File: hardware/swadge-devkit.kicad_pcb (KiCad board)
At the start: 2 copper layers, 63.7 x 89.4 mm, 65 parts, among them J1 USB_B_Micro, SW1 SW_SPDT, SW2 4-1437565-2, SW3 4-1437565-2, SW4 4-1437565-2, SW5 4-1437565-2, U1 ESP-13-WROOM-02D, U2 MCP6001-OT, U3 MSA300, U4 AP1117-33, U5 BUS_PCIexpress, U6 DISP_OLED_UG-2864HSWEG01, U7 SAO, U9 MMA8452Q

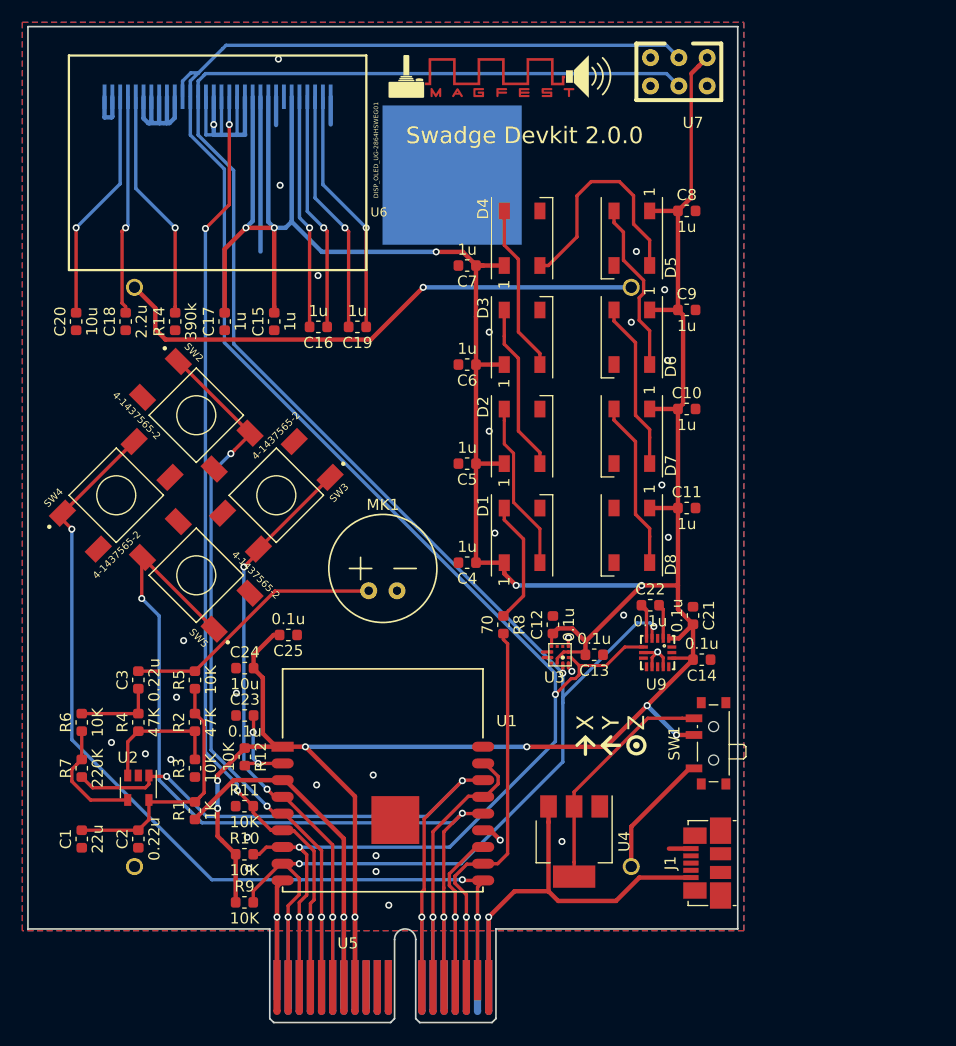
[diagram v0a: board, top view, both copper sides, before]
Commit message: Added Gainsil GS321-TR opamp
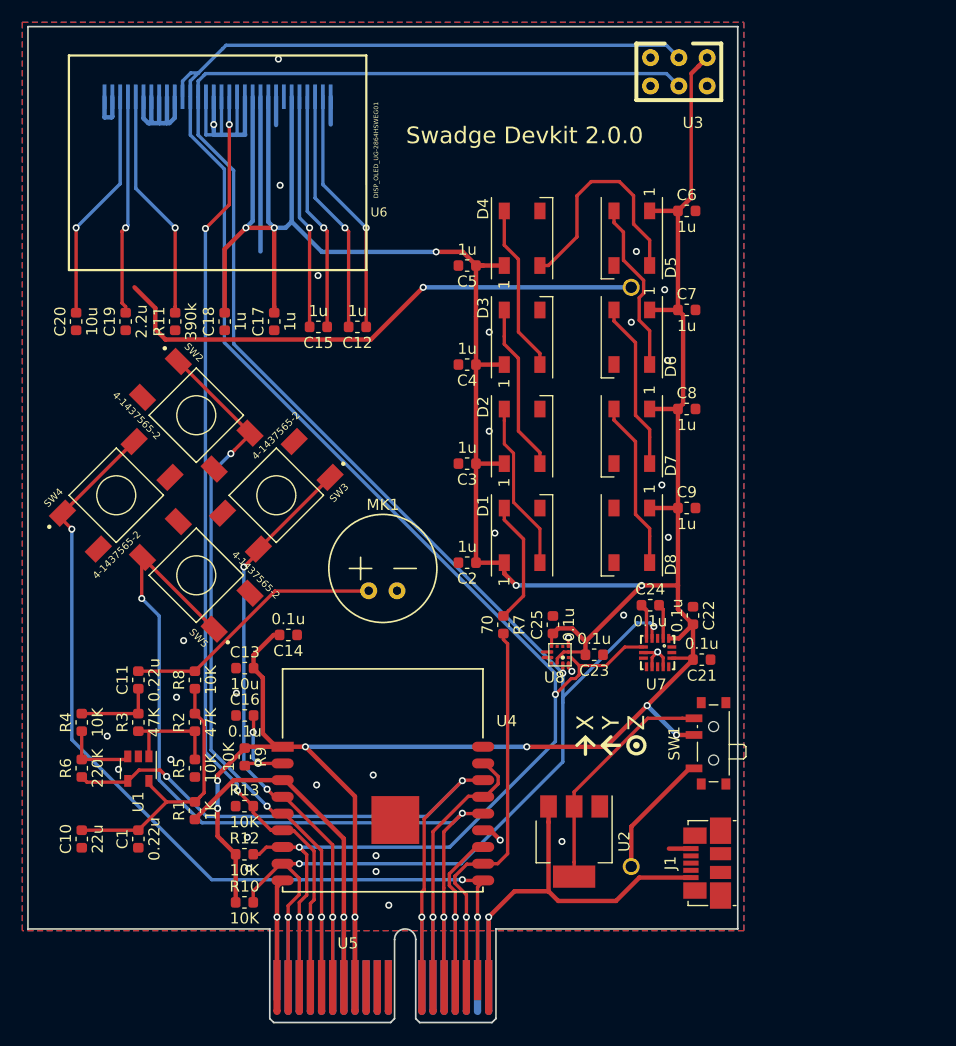
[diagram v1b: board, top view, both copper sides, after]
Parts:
- removed BT1: Battery, Swadge_Parts:2460
- removed the U2 at (123.4, 126.2)
- removed svg2mod: G***, Swadge_Parts:pcb_color_swatches
- removed svg2mod: G***, Swadge_Parts:MAGFEST_logo_centered_final
- added U1: GS321-TR, Swadge_Parts:SOT-23-5, F.Cu at (123.4, 124.5)
- renumbered C2 to C1, C1 to C10, C3 to C11, C19 to C12, C24 to C13, C25 to C14, C16 to C15, C23 to C16, C15 to C17, C17 to C18, C18 to C19, C4 to C2, C14 to C21, C21 to C22, C13 to C23, C22 to C24, C12 to C25, C5 to C3, C6 to C4, C7 to C5, C8 to C6, C9 to C7, C10 to C8, C11 to C9, R9 to R10, R14 to R11, R10 to R12, R11 to R13, R4 to R3, R6 to R4, R3 to R5, R7 to R6, R8 to R7, R5 to R8, R12 to R9, U4 to U2, U7 to U3, U1 to U4, U9 to U7, U3 to U8
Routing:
- net Net-(R4-Pad1): track 10.6 -> 6.41 mm
- net Net-(R2-Pad1): track 12.0 -> 9.89 mm
- net Net-(C1-Pad2): track 23.2 -> 24.2 mm
- net ADC_PIN: track 66.6 -> 65.7 mm

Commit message: Added back missing battery, PCB art
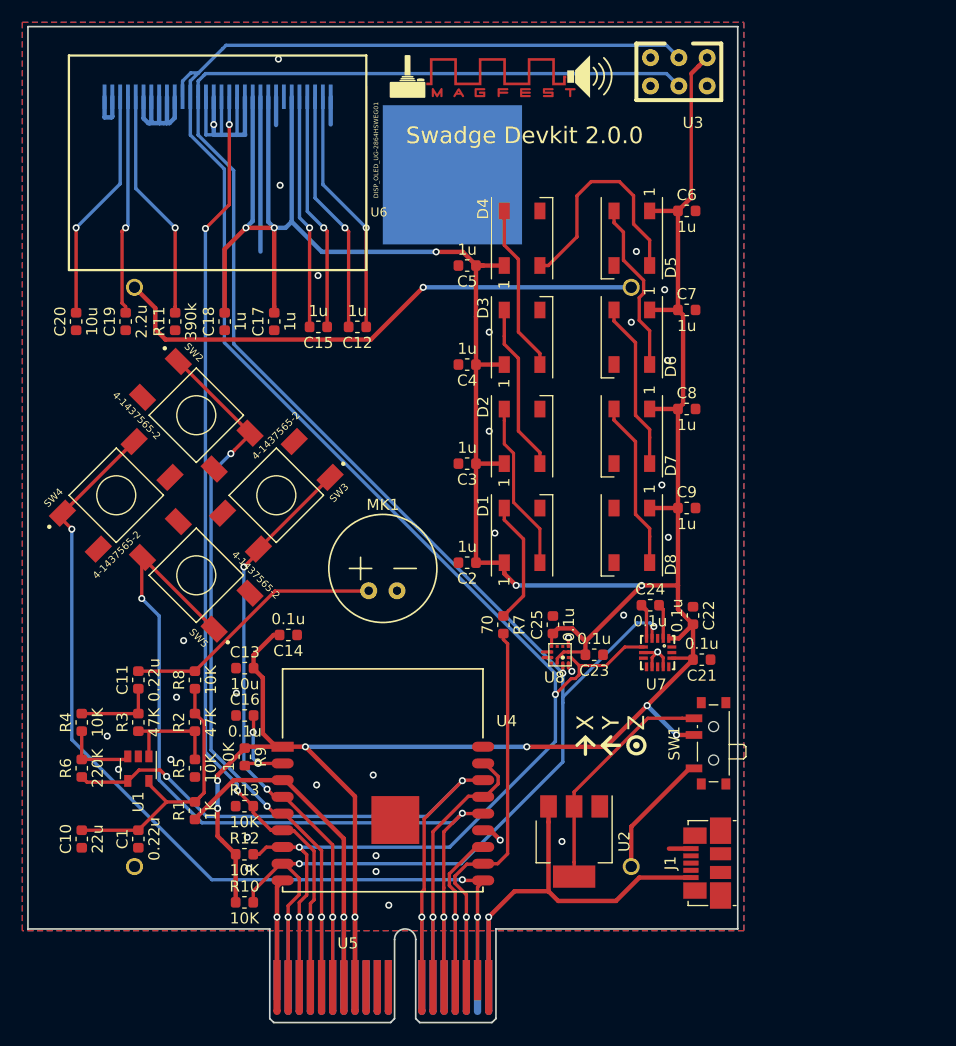
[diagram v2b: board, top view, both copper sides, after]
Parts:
- added BT1: Battery, Swadge_Parts:2460, B.Cu at (123.1, 107.3)
- added svg2mod: G***, Swadge_Parts:pcb_color_swatches, B.Cu at (157.9, 71.2)
- added svg2mod: G***, Swadge_Parts:MAGFEST_logo_centered_final, F.Cu at (156.0, 62.4)

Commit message: Added QMA6981 to the devkit
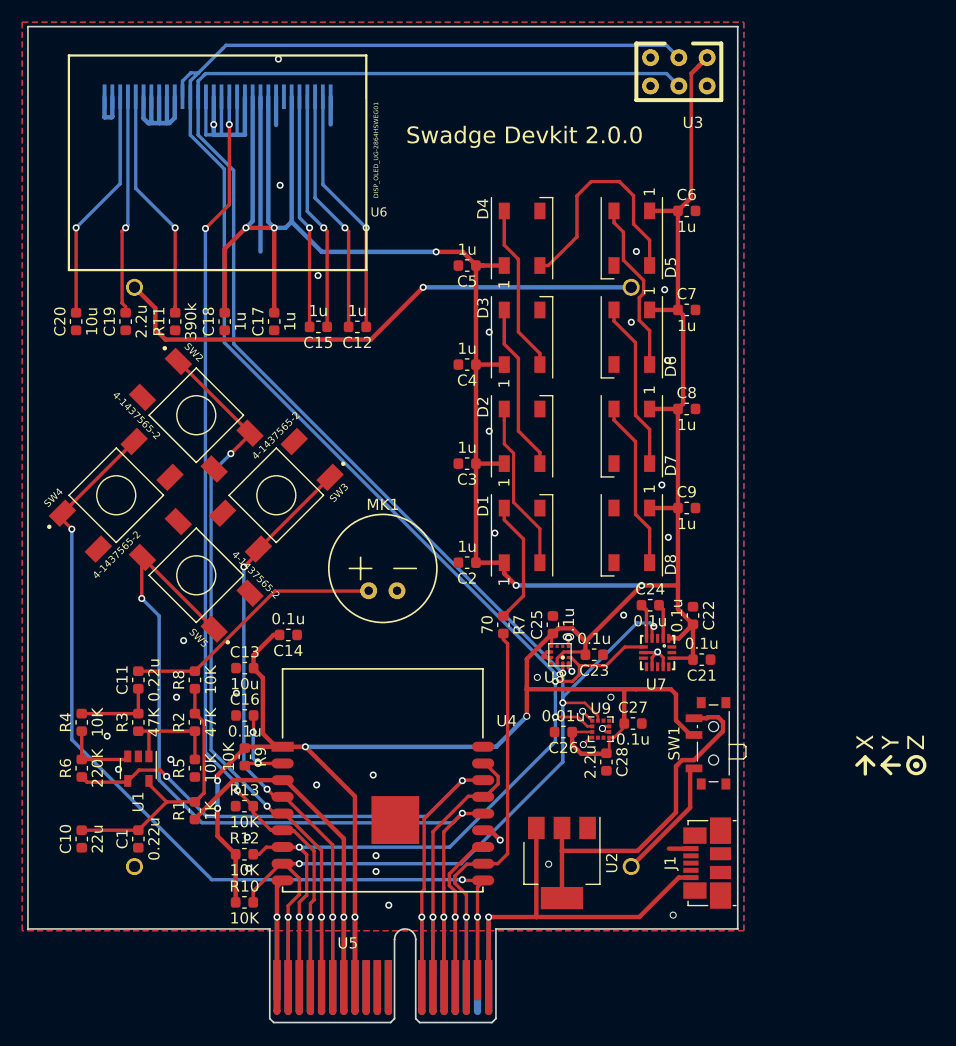
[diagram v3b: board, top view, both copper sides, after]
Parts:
- removed svg2mod: G***, Swadge_Parts:pcb_color_swatches
- removed svg2mod: G***, Swadge_Parts:MAGFEST_logo_centered_final
- added C26: 0.01u, Swadge_Parts:C_0603_1608Metric, F.Cu at (161.6, 121.2)
- added C27: 0.1u, Swadge_Parts:C_0603_1608Metric, F.Cu at (167.8, 120.5)
- added C28: 2.2u, Swadge_Parts:C_0603_1608Metric, F.Cu at (165.5, 123.9)
- added U9: QMA6981, Swadge_Parts:LGA-12_2x2mm_P0.5mm, F.Cu at (164.9, 121.0)
- moved U2 2.22 mm to (161.5, 133.0)
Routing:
- net +3V3: track 322.1 -> 338.9 mm, vias 12 -> 10
- net Net-(SW1-Pad3): track 21.1 -> 31.3 mm
- net SCL: track 184.0 -> 188.0 mm, vias 4 -> 5
- net GND: track 88.1 -> 92.0 mm, vias 33 -> 39
- net SDA: track 183.3 -> 186.3 mm, vias 3 -> 4
- net Net-(BT2-Pad1): track 11.4 -> 10.8 mm
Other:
- net class xThin added: clearance 0.19558, trace_width 0.2, via_dia 0.635, via_drill 0.3556

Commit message: Fixed silkscreen
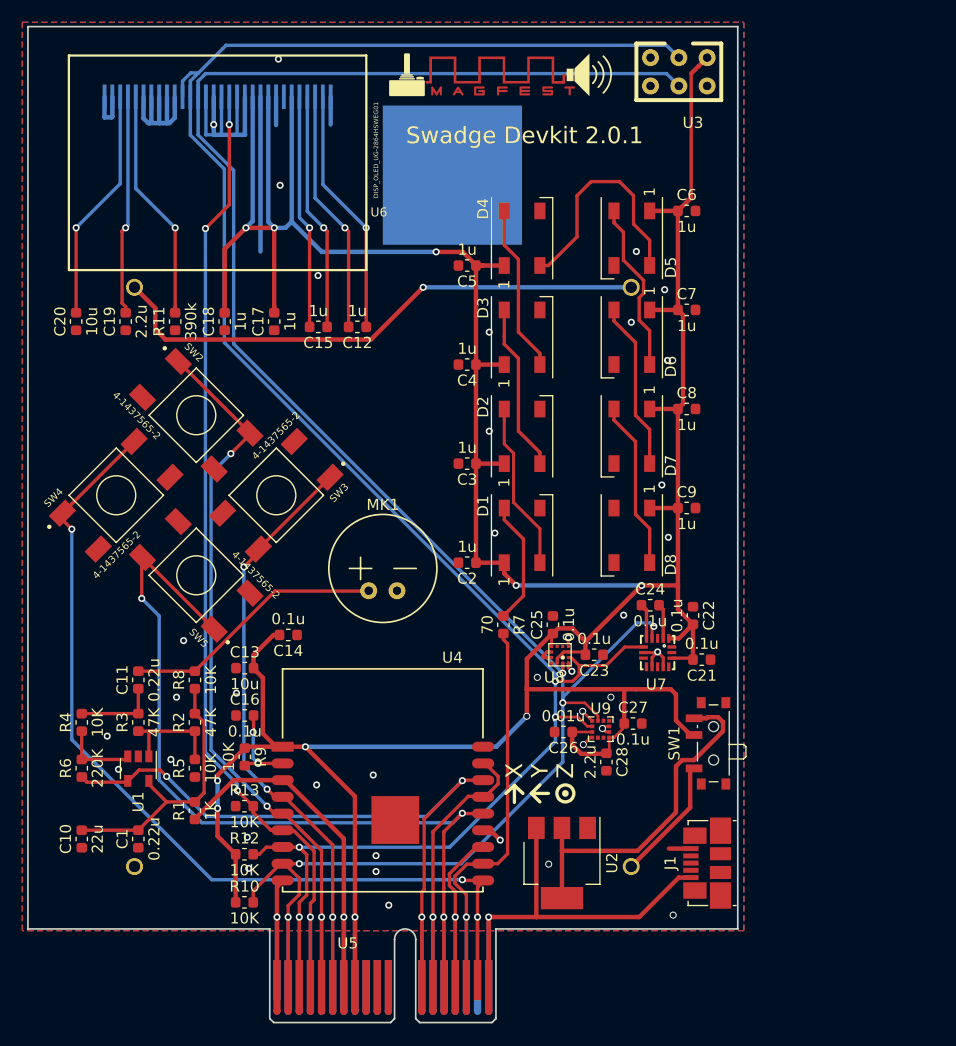
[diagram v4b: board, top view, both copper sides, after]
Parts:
- added svg2mod: G***, Swadge_Parts:pcb_color_swatches, B.Cu at (157.9, 71.2)
- added svg2mod: G***, Swadge_Parts:MAGFEST_logo_centered_final, F.Cu at (156.0, 62.2)
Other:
- board text added: "Swadge Devkit 2.0.1"
- board text removed: "Swadge Devkit 2.0.0"

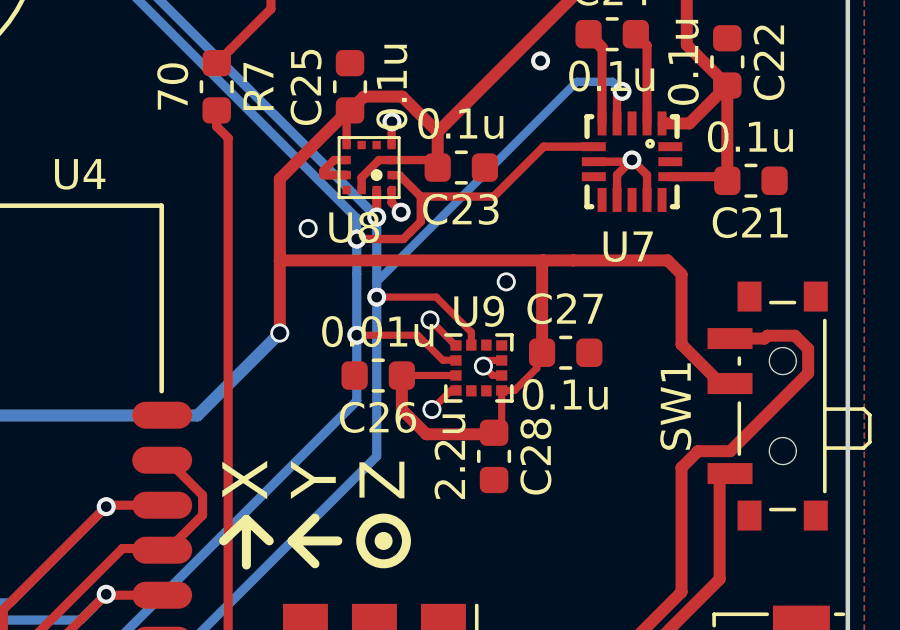
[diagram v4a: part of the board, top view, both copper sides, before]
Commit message: Added new QMA6981 footprint, no more DRC errors
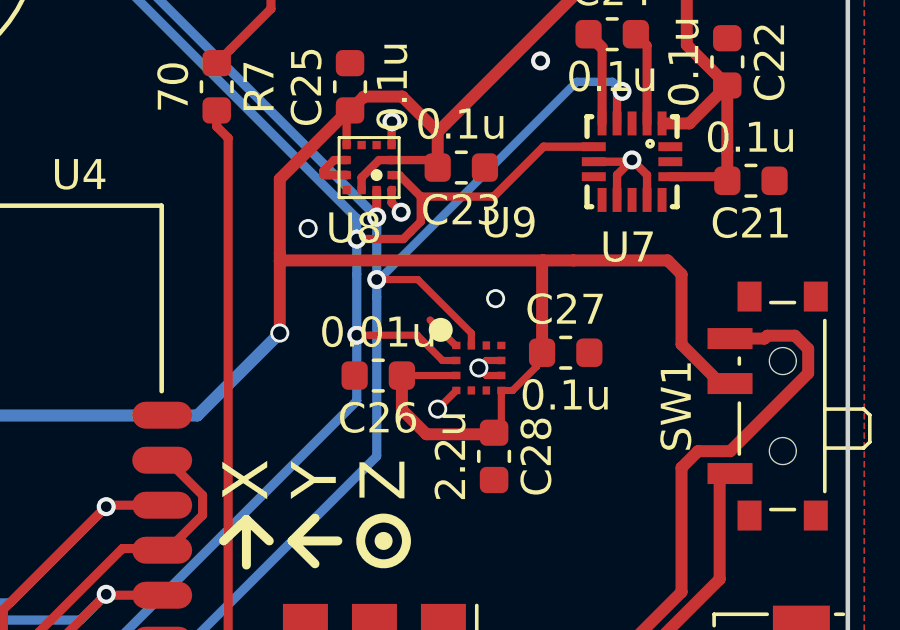
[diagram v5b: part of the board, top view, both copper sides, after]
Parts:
- U9: footprint Swadge_Parts:LGA-12_2x2mm_P0.5mm -> Swadge_Parts:QMA6981
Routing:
- net GND: track 92.0 -> 92.1 mm, vias 39 -> 38

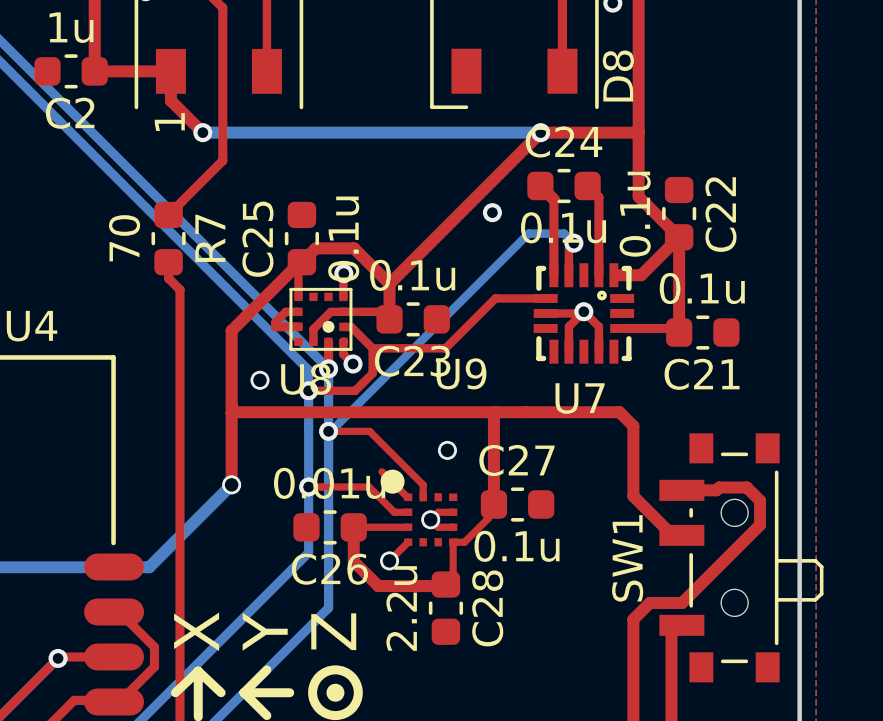
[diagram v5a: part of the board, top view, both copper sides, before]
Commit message: Fixed DRC error, silkscreen
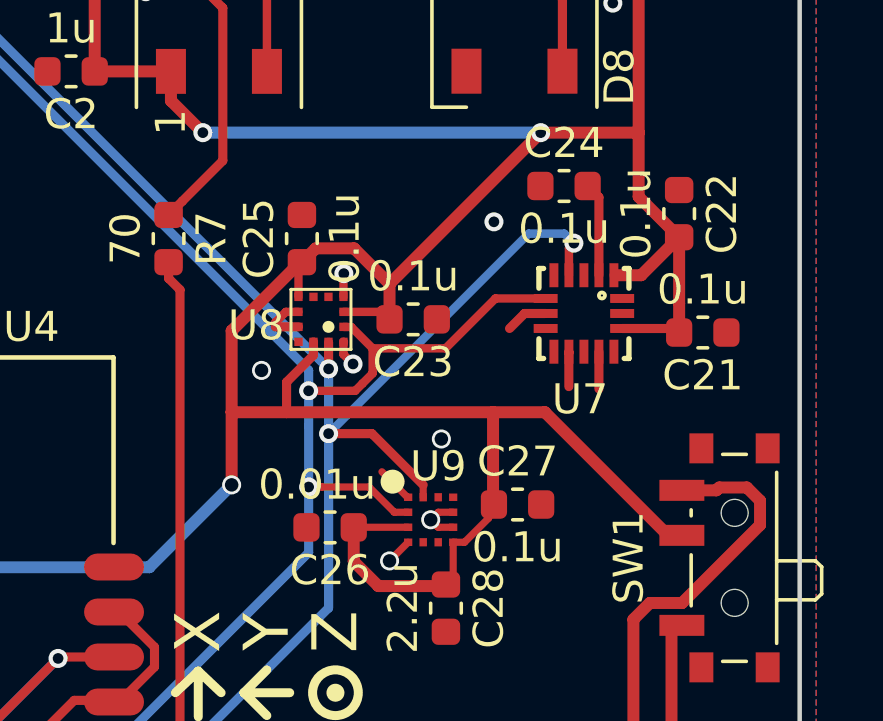
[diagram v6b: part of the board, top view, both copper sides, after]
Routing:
- net GND: track 92.1 -> 88.4 mm, vias 38 -> 37
